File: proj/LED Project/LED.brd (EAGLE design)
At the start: 58.4 x 32.7 mm, 19 parts, among them J3 AVR_SPI_PROG_3X2NS, U2 ATMEGA328P_MLF, Y1 16MHz

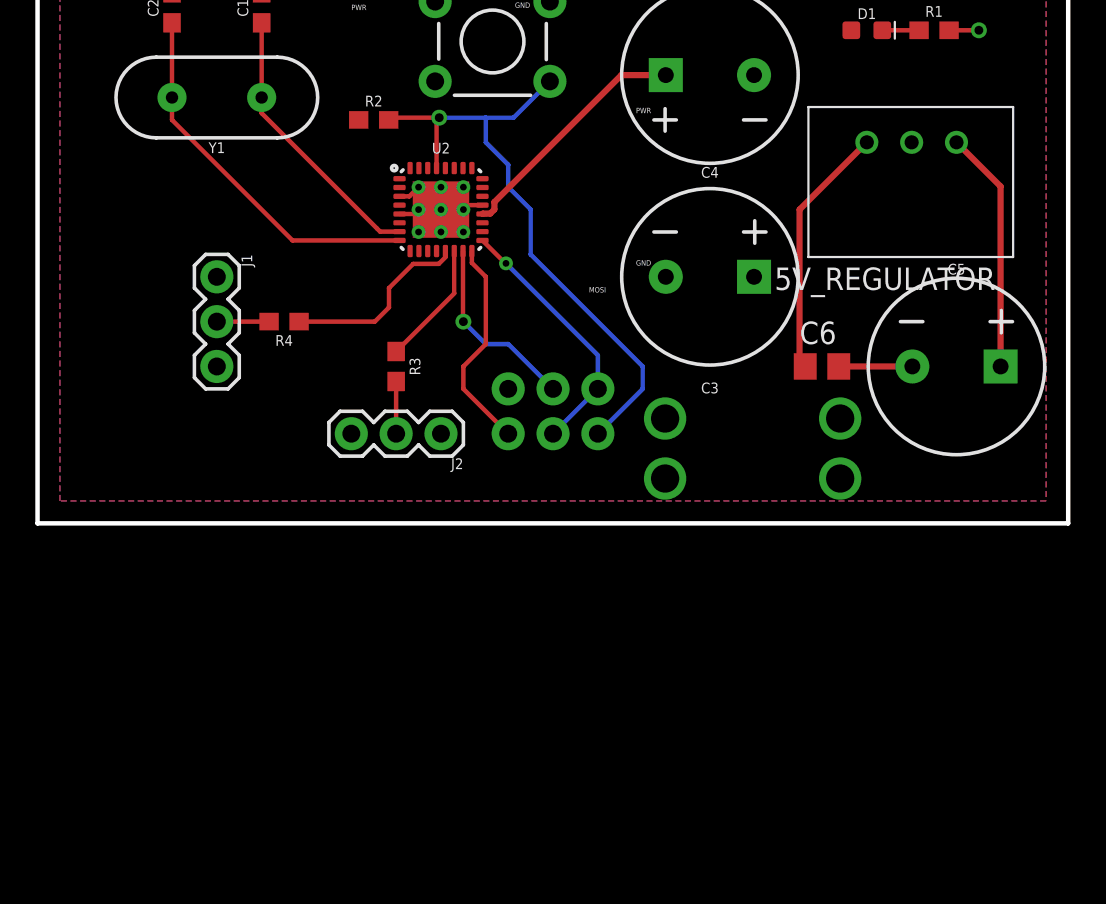
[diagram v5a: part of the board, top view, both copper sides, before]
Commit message: Reorganzing the Schematic and adding documentation
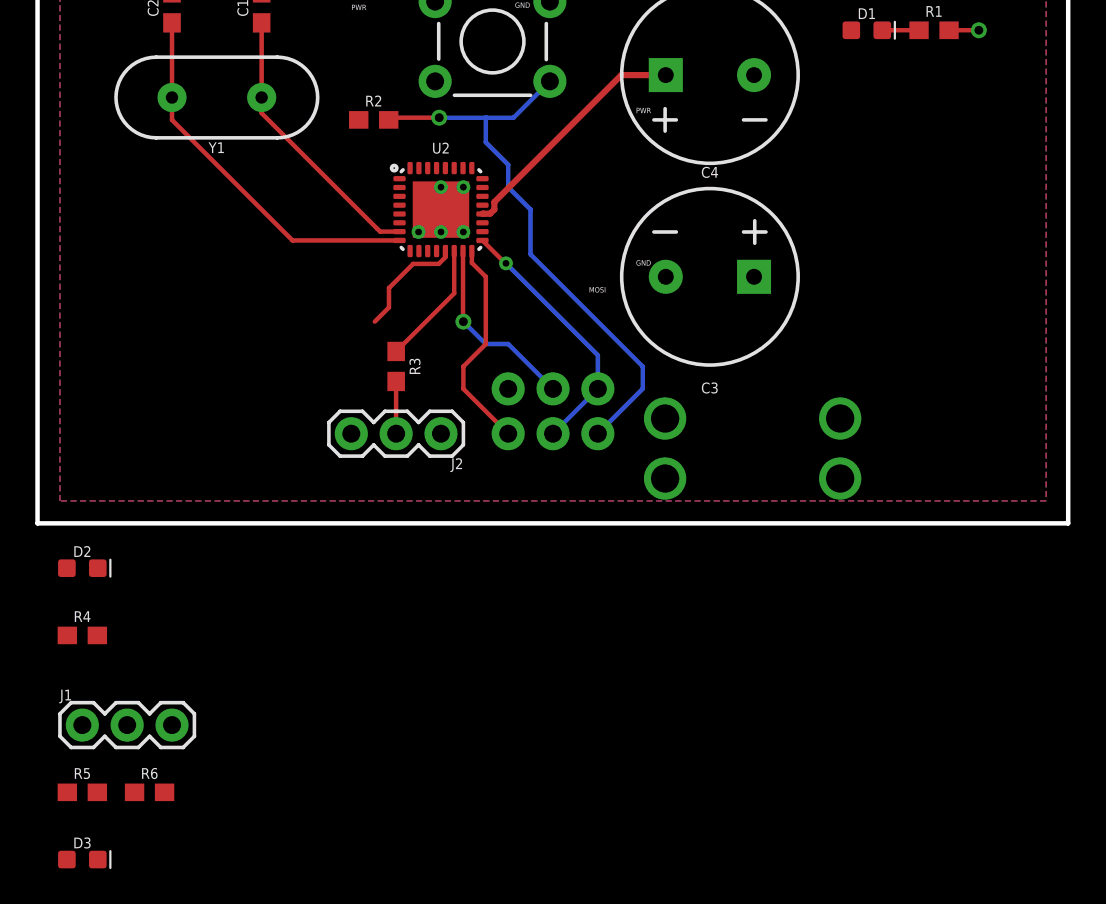
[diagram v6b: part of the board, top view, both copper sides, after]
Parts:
- removed 5V_REGULATOR: R-78E5.0-1.0, SparkFun-IC-Power:DC-DC_CONVERTER_78XX
- removed C5: 10uF, SparkFun-Capacitors:CPOL-RADIAL-5MM-10MM
- removed C6: 10uF, rcl:C0805
- added D2, D3: GREEN, SparkFun-LED:LED-0603
- added R5: 400, SparkFun-Resistors:0603
- added R6: 200, SparkFun-Resistors:0603
- C3: value 1mF -> 1000uF
- R4: value 400 -> 200
- moved J1 26.5 mm to (52.1, -11.4), turned to 0 degrees
- moved R4 21.1 mm to (52.1, -6.35), turned to 0 degrees
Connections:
- removed net 9V: 5V_REGULATOR.VIN, C5.+
- new net 5V: FUSE.P$3, FUSE.P$4
- new net N$2: D2.C, R4.2
- new net N$3: J2.3, R4.1
- new net N$4: D3.C, R6.2
- net DATA1: now also R5.2; no longer R4.2
- net GND: no longer 5V_REGULATOR.GND, C5.-, C6.2
- net N$5: now also J1.3, R6.1; no longer 5V_REGULATOR.VOUT, C6.1, FUSE.P$3, FUSE.P$4
- net NP1: now also R5.1; no longer R4.1
- net VCC: now also D2.A, D3.A; no longer J1.3, J2.3
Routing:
- net N$5: track 14.4 -> 0.00 mm
- net 9V: track 13.7 -> 0.00 mm
- net GND: track 14.6 -> 6.80 mm, vias 11 -> 7
- net NP1: track 10.8 -> 6.50 mm
- net DATA1: track 2.96 -> 0.00 mm
- net RST: track 35.6 -> 32.9 mm

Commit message: Documentation + style changes
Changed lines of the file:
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@@
 <?xml version="1.0" encoding="utf-8"?>
 <!DOCTYPE eagle SYSTEM "eagle.dtd">
-<eagle version="9.1.3">
+<eagle version="9.2.2">
 <drawing>
 <settings>
@@
 </element>
 <element name="FUSE" library="IGVC-Misc" package="FUSE_HOLDER" value="3.6A" x="85.09" y="2.54" smashed="yes"/>
-<element name="D2" library="SparkFun-LED" library_urn="urn:adsk.eagle:library:529" package="LED-0603" package3d_urn="urn:adsk.eagle:package:39354/1" value="GREEN" x="52.07" y="-2.54">
+<element name="D2" library="SparkFun-LED" library_urn="urn:adsk.eagle:library:529" package="LED-0603" package3d_urn="urn:adsk.eagle:package:39354/1" value="GREEN" x="52.07" y="-2.54" smashed="yes">
+<attribute name="NAME" x="52.07" y="-1.905" size="0.6096" layer="25" font="vector" ratio="20" align="bottom-center"/>
 <attribute name="PROD_ID" value="DIO-00821" x="52.07" y="-2.54" size="1.778" layer="27" display="off"/>
-</element>
-<element name="R4" library="SparkFun-Resistors" library_urn="urn:adsk.eagle:library:532" package="0603" package3d_urn="urn:adsk.eagle:package:39650/1" value="200" x="52.07" y="-6.35">
+<attribute name="VALUE" x="52.07" y="-3.175" size="0.6096" layer="27" font="vector" ratio="20" align="top-center"/>
+</element>
+<element name="R4" library="SparkFun-Resistors" library_urn="urn:adsk.eagle:library:532" package="0603" package3d_urn="urn:adsk.eagle:package:39650/1" value="200" x="52.07" y="-6.35" smashed="yes">
+<attribute name="NAME" x="52.07" y="-5.588" size="0.6096" layer="25" font="vector" ratio="20" align="bottom-center"/>
 <attribute name="PROD_ID" value="RES-07869" x="52.07" y="-6.35" size="1.778" layer="27" display="off"/>
-</element>
-<element name="J1" library="SparkFun-Connectors" library_urn="urn:adsk.eagle:library:513" package="1X03" package3d_urn="urn:adsk.eagle:package:38063/1" value="" x="52.07" y="-11.43">
+<attribute name="VALUE" x="52.07" y="-7.112" size="0.6096" layer="27" font="vector" ratio="20" align="top-center"/>
+</element>
+<element name="J1" library="SparkFun-Connectors" library_urn="urn:adsk.eagle:library:513" package="1X03" package3d_urn="urn:adsk.eagle:package:38063/1" value="" x="52.07" y="-11.43" smashed="yes">
+<attribute name="NAME" x="50.8" y="-10.033" size="0.6096" layer="25" font="vector" ratio="20"/>
 <attribute name="SPICEPREFIX" value="J" x="52.07" y="-11.43" size="1.778" layer="27" display="off"/>
-</element>
-<element name="R5" library="SparkFun-Resistors" library_urn="urn:adsk.eagle:library:532" package="0603" package3d_urn="urn:adsk.eagle:package:39650/1" value="400" x="52.07" y="-15.24">
+<attribute name="VALUE" x="50.8" y="-13.462" size="0.6096" layer="27" font="vector" ratio="20"/>
+</element>
+<element name="R5" library="SparkFun-Resistors" library_urn="urn:adsk.eagle:library:532" package="0603" package3d_urn="urn:adsk.eagle:package:39650/1" value="400" x="52.07" y="-15.24" smashed="yes">
+<attribute name="NAME" x="52.07" y="-14.478" size="0.6096" layer="25" font="vector" ratio="20" align="bottom-center"/>
 <attribute name="PROD_ID" value="RES-07869" x="52.07" y="-15.24" size="1.778" layer="27" display="off"/>
-</element>
-<element name="D3" library="SparkFun-LED" library_urn="urn:adsk.eagle:library:529" package="LED-0603" package3d_urn="urn:adsk.eagle:package:39354/1" value="GREEN" x="52.07" y="-19.05">
+<attribute name="VALUE" x="52.07" y="-16.002" size="0.6096" layer="27" font="vector" ratio="20" align="top-center"/>
+</element>
+<element name="D3" library="SparkFun-LED" library_urn="urn:adsk.eagle:library:529" package="LED-0603" package3d_urn="urn:adsk.eagle:package:39354/1" value="GREEN" x="52.07" y="-19.05" smashed="yes">
+<attribute name="NAME" x="52.07" y="-18.415" size="0.6096" layer="25" font="vector" ratio="20" align="bottom-center"/>
 <attribute name="PROD_ID" value="DIO-00821" x="52.07" y="-19.05" size="1.778" layer="27" display="off"/>
-</element>
-<element name="R6" library="SparkFun-Resistors" library_urn="urn:adsk.eagle:library:532" package="0603" package3d_urn="urn:adsk.eagle:package:39650/1" value="200" x="55.88" y="-15.24">
+<attribute name="VALUE" x="52.07" y="-19.685" size="0.6096" layer="27" font="vector" ratio="20" align="top-center"/>
+</element>
+<element name="R6" library="SparkFun-Resistors" library_urn="urn:adsk.eagle:library:532" package="0603" package3d_urn="urn:adsk.eagle:package:39650/1" value="200" x="55.88" y="-15.24" smashed="yes">
+<attribute name="NAME" x="55.88" y="-14.478" size="0.6096" layer="25" font="vector" ratio="20" align="bottom-center"/>
 <attribute name="PROD_ID" value="RES-07869" x="52.07" y="-22.86" size="1.778" layer="27" display="off"/>
+<attribute name="VALUE" x="55.88" y="-16.002" size="0.6096" layer="27" font="vector" ratio="20" align="top-center"/>
 </element>
 </elements>
@@
 <contactref element="FUSE" pad="P$1"/>
 <contactref element="FUSE" pad="P$2"/>
-<contactref element="D1" pad="A"/>
 <contactref element="D2" pad="A"/>
 <contactref element="D3" pad="A"/>
+<contactref element="D1" pad="A"/>
+<wire x1="90.13" y1="13.97" x2="95.643" y2="27.94" width="0" layer="19" extent="1-1"/>
+<wire x1="85.09" y1="5.94" x2="90.13" y2="13.97" width="0" layer="19" extent="1-1"/>
+<wire x1="85.09" y1="2.54" x2="85.09" y2="5.94" width="0" layer="19" extent="1-1"/>
+<wire x1="76.2" y1="7.62" x2="85.09" y2="5.94" width="0" layer="19" extent="1-1"/>
+<wire x1="74.74" y1="16.53" x2="76.2" y2="7.62" width="0" layer="19" extent="1-1"/>
+<wire x1="70.04" y1="17.03" x2="74.74" y2="16.53" width="0" layer="19" extent="1-1"/>
+<wire x1="70.04" y1="18.03" x2="70.04" y2="17.03" width="0" layer="19" extent="1-1"/>
+<wire x1="67.73" y1="22.86" x2="70.04" y2="18.03" width="0" layer="19" extent="1-1"/>
+<wire x1="51.193" y1="-2.54" x2="76.2" y2="7.62" width="0" layer="19" extent="1-1"/>
 <wire x1="51.193" y1="-19.05" x2="51.193" y2="-2.54" width="0" layer="19" extent="1-1"/>
-<wire x1="76.2" y1="7.62" x2="51.193" y2="-2.54" width="0" layer="19" extent="1-1"/>
 </signal>
 <signal name="MISO">
